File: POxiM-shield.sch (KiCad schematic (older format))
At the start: 77 parts, among them Q1 Q_NMOS_DGS, Q10 Q_NMOS_DGS, Q13 Q_NPN_BCE, Q2 Q_NMOS_DGS, Q3 Q_NMOS_DGS, Q4 Q_NMOS_DGS, Q5 Q_NMOS_DGS, Q6 Q_NMOS_DGS, Q7 Q_NMOS_DGS, Q8 Q_NMOS_DGS, Q9 Q_NMOS_DGS, U1 LM324, U2 LM324, U3 LM324, U4 LM324

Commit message: Put design options in separate sheets
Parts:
- removed C1, C10, C11, C12 (x2), C14, C16, C17, C18, C2, C3, C4, C5, C6, C7, C8, C9, C? (x3): 470nF, symbol Device:C
- removed C13, C?: 10nF, symbol Device:C
- removed D1, D2, D3, D4, D5, D6: D_Photo, symbol Device:D_Photo
- removed Q1, Q10, Q2, Q3, Q4, Q5, Q6, Q7, Q8, Q9, Q? (x3): Q_NMOS_DGS, symbol Device:Q_NMOS_DGS
- removed Q13: Q_NPN_BCE, symbol Device:Q_NPN_BCE
- removed R1, R10, R11, R12, R17, R19, R2, R21, R22, R23, R24, R25, R26, R27, R28, R29, R3, R5, R6, R7, R8, R9, R?: R_US, symbol Device:R_US
- removed R4: 220kΩ, symbol Device:R_US
- removed U1, U2, U3, U4: LM324, symbol Amplifier_Operational:LM324
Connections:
- net labels removed: RST, Sample, ToADC, ToOptionalADC\comparator
- wire segments 250 -> 23
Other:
- note removed: "0 to 3.3V range"
- note removed: "Consider replacing\nopamp with transistor"
- note removed: "Dual MOSFET or\nSingle MOSFET forces\nLED brightness control"
- note removed: "Requires brighness\ncontrol of LEDs"
- note removed: "Time freezing filter vs\nsample and hold"
- note removed: "f_c = 6Hz to 9Hz"
- moved on the sheet: A1, C?, D7, R14, R15, R16, R20

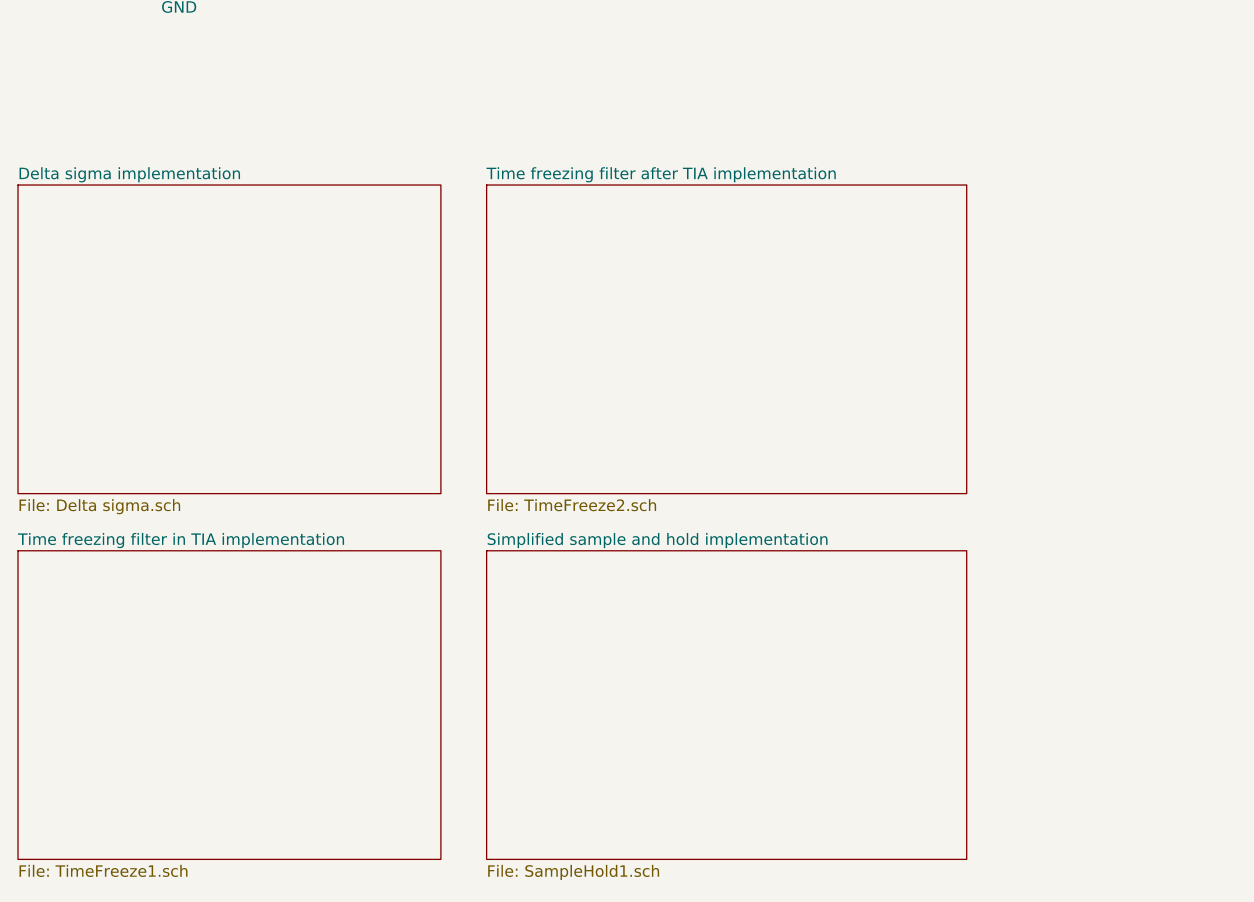
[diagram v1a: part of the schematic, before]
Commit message: Modify delta sigma for noise shaping with ADC, set analysis goals and analyse up to aliasing
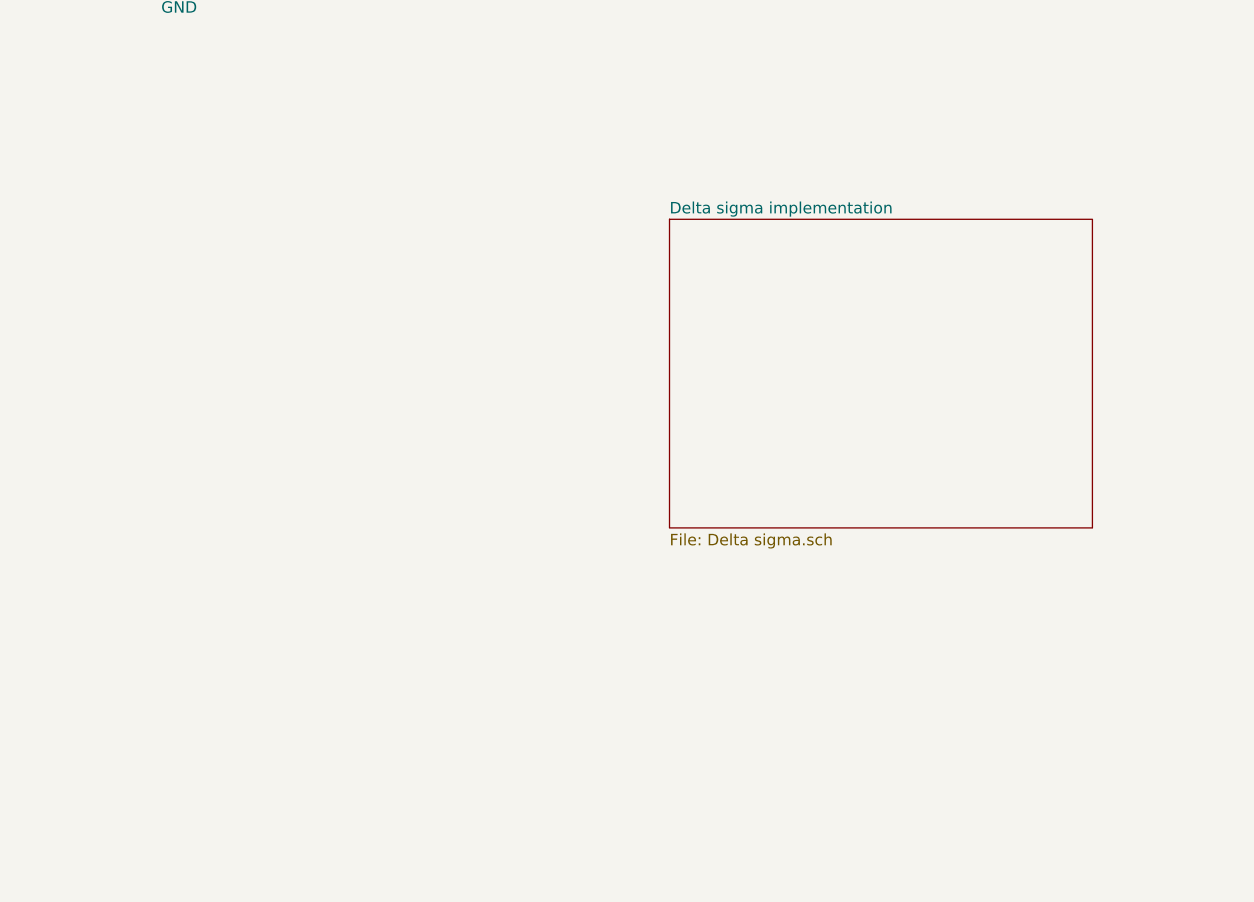
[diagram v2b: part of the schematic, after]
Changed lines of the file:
@@
 $Descr A4 11693 8268
 encoding utf-8
-Sheet 1 5
+Sheet 1 2
 Title "POxiM test shield"
 Date "2020-04-24"
@@
 	7300 2200 7300 2300
 $Sheet
-S 850  4150 1850 1350
+S 3700 4300 1850 1350
 U 5EB36E07
 F0 "Delta sigma implementation" 50
 F1 "Delta sigma.sch" 50
 $EndSheet
-$Sheet
-S 2900 4150 2100 1350
-U 5EBF2A40
-F0 "Time freezing filter after TIA implementation" 50
-F1 "TimeFreeze2.sch" 50
-$EndSheet
-$Sheet
-S 850  5750 1850 1350
-U 5EBFF598
-F0 "Time freezing filter in TIA implementation" 50
-F1 "TimeFreeze1.sch" 50
-$EndSheet
-$Sheet
-S 2900 5750 2100 1350
-U 5EC55EF3
-F0 "Simplified sample and hold implementation" 50
-F1 "SampleHold1.sch" 50
-$EndSheet
 $EndSCHEMATC
